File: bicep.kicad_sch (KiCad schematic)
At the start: 59 parts, among them J1 DEBUG, J10 BATT, J11 USB_B_Micro, J12 BATT, J2 QWIIC, J3 QWIIC, J4 I2C, J5 SERIAL1, J6 SERIAL2, J7 ANALOG, J8 MISC, J9 DATA, Q1 2N7002, Q2 DMG3401, SW1 RESET, SW2 POWER, U1 ATSAMD21G18A-A, U2 RFM95W-915S2, U3 MCP73831-2, U4 AP2112K-3.3, Y1 32.768K-12.5p

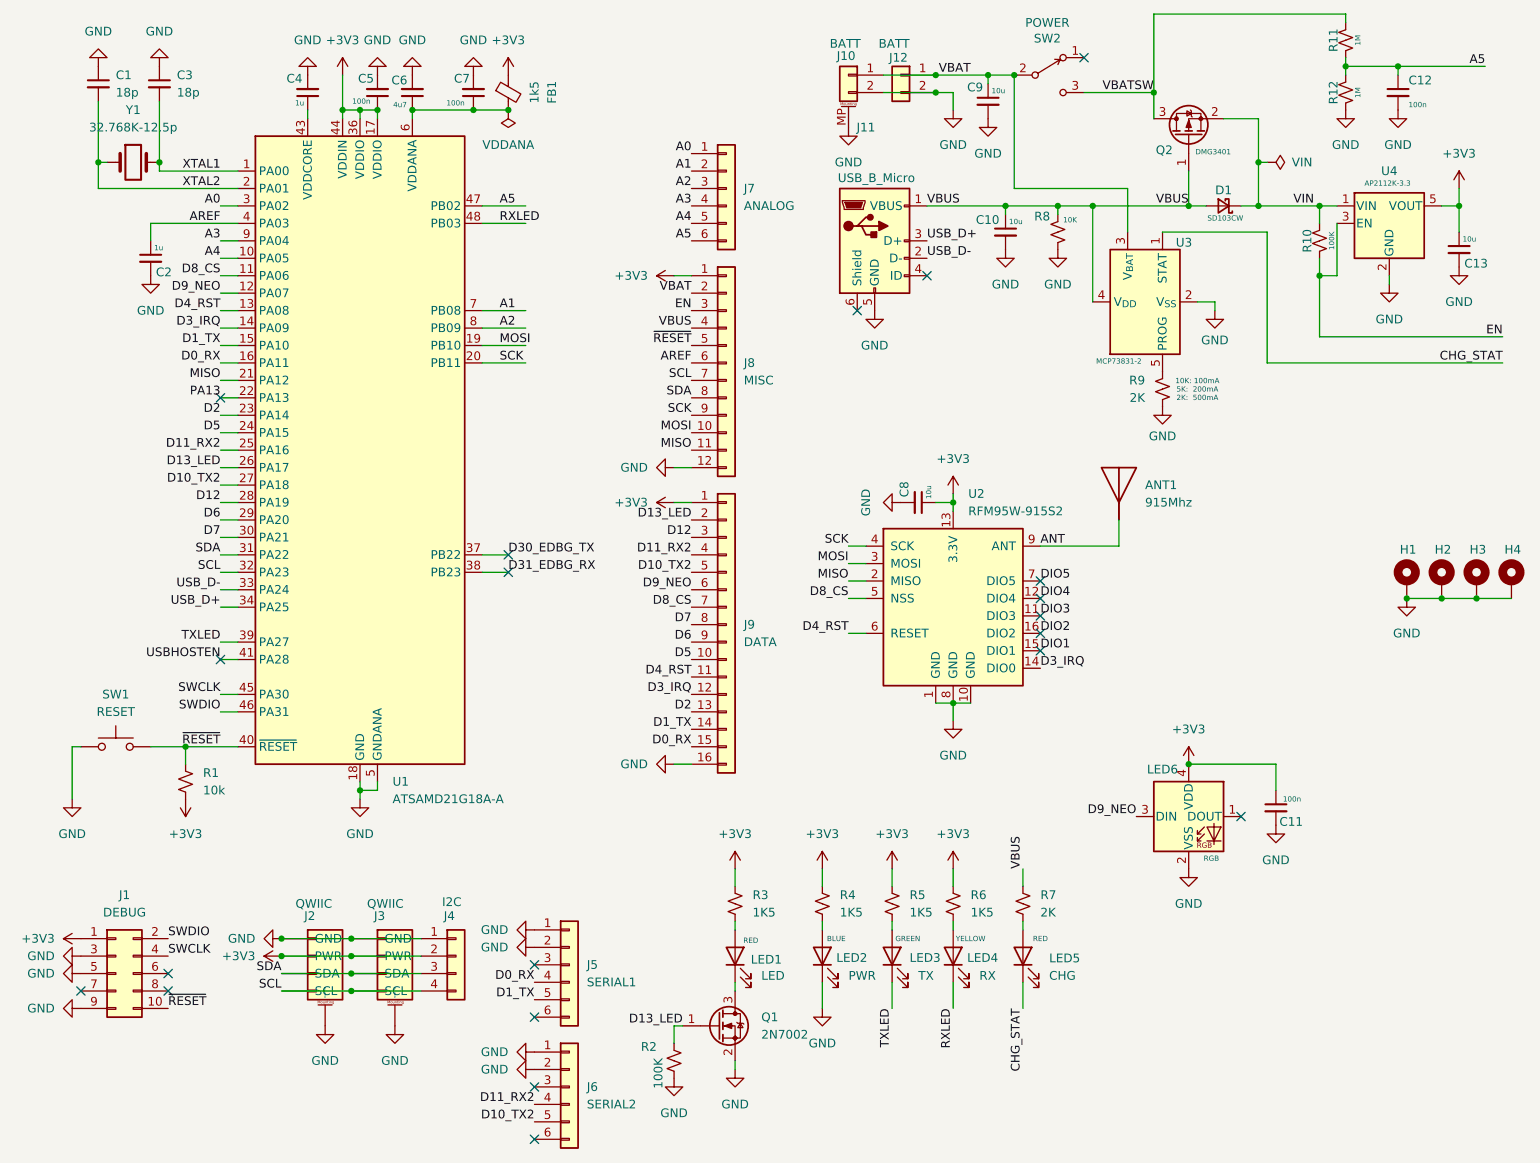
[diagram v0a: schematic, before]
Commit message: Added shroud to 3d rendering of Cortex Debug connector
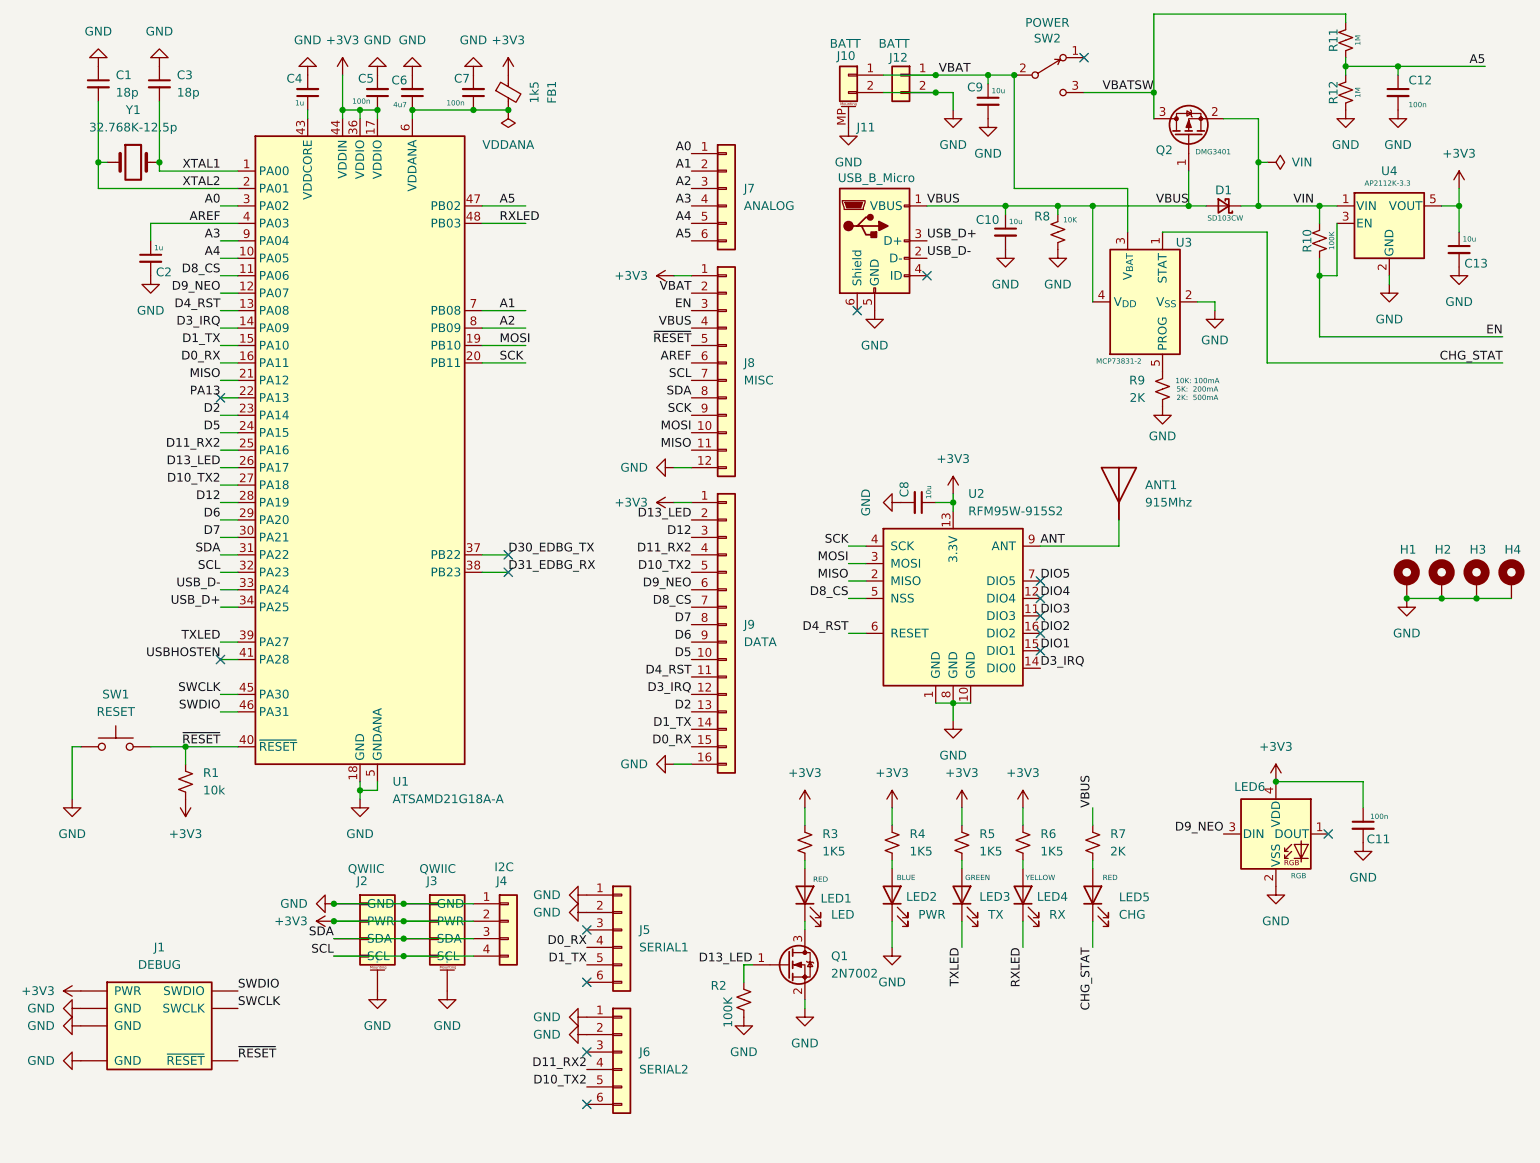
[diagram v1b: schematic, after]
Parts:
- J1: footprint Connector_PinHeader_1.27mm:PinHeader_2x05_P1.27mm_Vertical -> MyLib:CortexDebug; symbol Connector_Generic:Conn_02x05_Odd_Even -> MyLib:CortexDebug
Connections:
- no-connect marks 20 -> 17
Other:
- moved on the sheet: C11, J2, J3, J4, J5, J6, LED1, LED2, LED3, LED4, LED5, LED6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
